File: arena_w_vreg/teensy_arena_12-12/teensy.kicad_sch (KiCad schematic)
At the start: 3 parts, among them J2 Conn_01x04_Pin, J3 Conn_01x04_Pin, U13 Teensy4.1

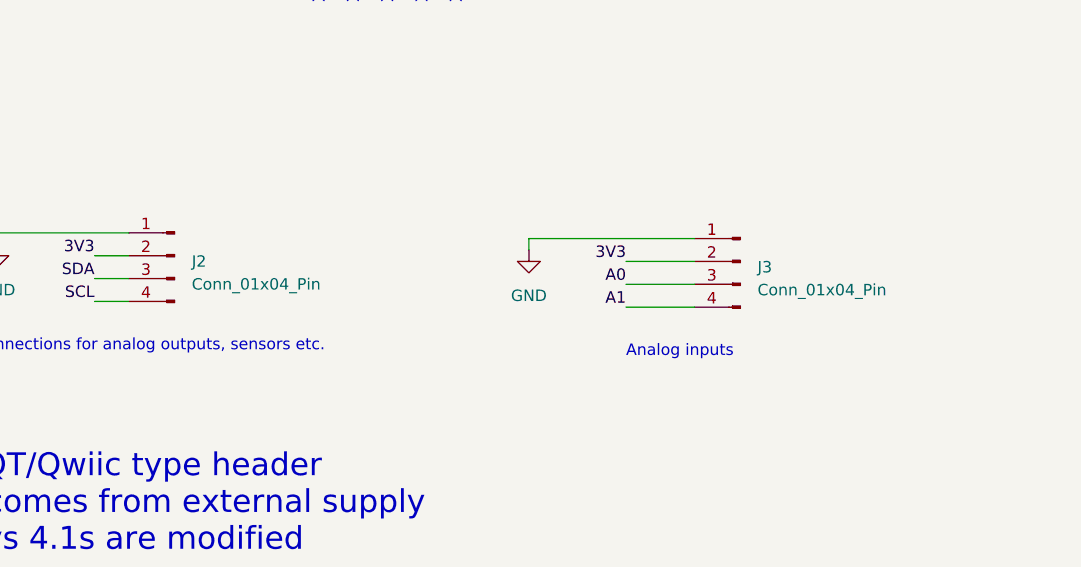
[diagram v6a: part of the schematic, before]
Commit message: Finished initial routing.
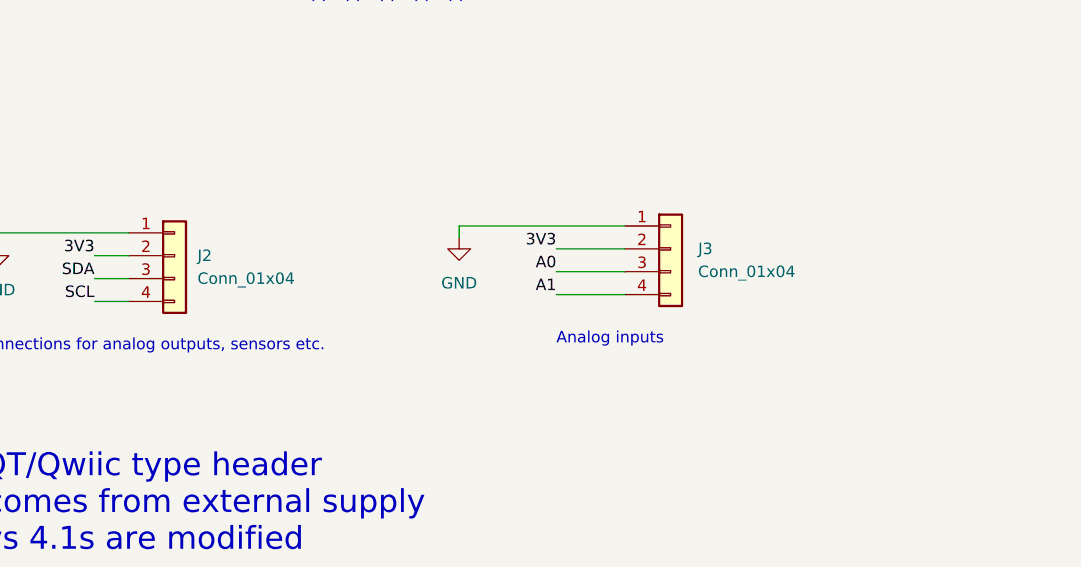
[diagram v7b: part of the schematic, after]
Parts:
- removed J2, J3: Conn_01x04_Pin, arena_custom:NS-Tech_Grove_1x04_P2mm_Horizontal, symbol Connector:Conn_01x04_Pin
- added J2, J3: Conn_01x04, Connector_JST:JST_SH_SM04B-SRSS-TB_1x04-1MP_P1.00mm_Horizontal, symbol Connector_Generic:Conn_01x04
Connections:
- net 3V3: now also J2.2 (Pin_2), J3.2 (Pin_2)
- net A0: now also J3.3 (Pin_3)
- net A1: now also J3.4 (Pin_4)
- net GND: now also J2.1 (Pin_1), J3.1 (Pin_1)
- net SCL: now also J2.4 (Pin_4)
- net SDA: now also J2.3 (Pin_3)
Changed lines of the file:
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@@
     (stroke (width 0) (type default))
   )
-  (wire (pts (xy 131.699 151.003) (xy 139.319 151.003))
+  (wire (pts (xy 123.952 149.606) (xy 131.572 149.606))
     (stroke (width 0) (type default))
   )
@@
     (stroke (width 0) (type default))
   )
-  (wire (pts (xy 120.904 148.463) (xy 120.904 149.733))
+  (wire (pts (xy 113.157 147.066) (xy 113.157 148.336))
     (stroke (width 0) (type default))
   )
@@
     (stroke (width 0) (type default))
   )
-  (wire (pts (xy 131.699 156.083) (xy 139.319 156.083))
+  (wire (pts (xy 123.952 154.686) (xy 131.572 154.686))
     (stroke (width 0) (type default))
   )
@@
     (stroke (width 0) (type default))
   )
-  (wire (pts (xy 120.904 148.463) (xy 139.319 148.463))
+  (wire (pts (xy 113.157 147.066) (xy 131.572 147.066))
     (stroke (width 0) (type default))
   )
@@
     (stroke (width 0) (type default))
   )
-  (wire (pts (xy 131.699 153.543) (xy 139.319 153.543))
+  (wire (pts (xy 123.952 152.146) (xy 131.572 152.146))
     (stroke (width 0) (type default))
   )
@@
     (effects (font (size 2.54 2.54)) (justify left bottom))
   )
-  (text "Analog inputs" (at 131.699 161.798 0)
+  (text "Analog inputs" (at 123.952 160.401 0)
     (effects (font (size 1.27 1.27)) (justify left bottom))
   )
@@
     (effects (font (size 1.27 1.27)) (justify left bottom))
   )
-  (label "3V3" (at 131.699 151.003 180) (fields_autoplaced)
+  (label "3V3" (at 123.952 149.606 180) (fields_autoplaced)
     (effects (font (size 1.27 1.27)) (justify right bottom))
   )
@@
     (effects (font (size 1.27 1.27)) (justify left bottom))
   )
-  (label "A1" (at 131.699 156.083 180) (fields_autoplaced)
+  (label "A1" (at 123.952 154.686 180) (fields_autoplaced)
     (effects (font (size 1.27 1.27)) (justify right bottom))
   )
@@
     (effects (font (size 1.27 1.27)) (justify left bottom))
   )
-  (label "A0" (at 131.699 153.543 180) (fields_autoplaced)
+  (label "A0" (at 123.952 152.146 180) (fields_autoplaced)
     (effects (font (size 1.27 1.27)) (justify right bottom))
   )
@@
     )
   )
-  (symbol (lib_id "Connector:Conn_01x04_Pin") (at 144.399 151.003 0) (mirror y) (unit 1)
+  (symbol (lib_id "Connector_Generic:Conn_01x04") (at 136.652 149.606 0) (unit 1)
     (in_bom yes) (on_board yes) (dnp no) (fields_autoplaced)
-    (property "Reference" "J3" (at 146.304 151.638 0)
-      (effects (font (size 1.27 1.27)) (justify right))
-    )
-    (property "Value" "Conn_01x04_Pin" (at 146.304 154.178 0)
-      (effects (font (size 1.27 1.27)) (justify right))
-    )
-    (property "Footprint" "arena_custom:NS-Tech_Grove_1x04_P2mm_Horizontal" (at 144.399 151.003 0)
-      (effects (font (size 1.27 1.27)) hide)
-    )
-    (property "Datasheet" "~" (at 144.399 151.003 0)
+    (property "Reference" "J3" (at 139.7 149.606 0)
+      (effects (font (size 1.27 1.27)) (justify left))
+    )
+    (property "Value" "Conn_01x04" (at 139.7 152.146 0)
+      (effects (font (size 1.27 1.27)) (justify left))
+    )
+    (property "Footprint" "Connector_JST:JST_SH_SM04B-SRSS-TB_1x04-1MP_P1.00mm_Horizontal" (at 136.652 149.606 0)
+      (effects (font (size 1.27 1.27)) hide)
+    )
+    (property "Datasheet" "~" (at 136.652 149.606 0)
       (effects (font (size 1.27 1.27)) hide)
     )
@@
     (instances
       (project "teensy_arena_12-12"
-        (path "/a2511654-3a17-43f1-8b9e-c45e375533dc"
-          (reference "J3") (unit 1)
-        )
         (path "/a2511654-3a17-43f1-8b9e-c45e375533dc/5b6d0be6-08d3-404a-9e9b-565c640343d3"
           (reference "J3") (unit 1)
@@
     )
   )
-  (symbol (lib_id "Connector:Conn_01x04_Pin") (at 81.534 150.368 0) (mirror y) (unit 1)
+  (symbol (lib_id "power:GND") (at 155.448 70.866 0) (mirror y) (unit 1)
     (in_bom yes) (on_board yes) (dnp no) (fields_autoplaced)
-    (property "Reference" "J2" (at 83.439 151.003 0)
-      (effects (font (size 1.27 1.27)) (justify right))
-    )
-    (property "Value" "Conn_01x04_Pin" (at 83.439 153.543 0)
-      (effects (font (size 1.27 1.27)) (justify right))
-    )
-    (property "Footprint" "arena_custom:NS-Tech_Grove_1x04_P2mm_Horizontal" (at 81.534 150.368 0)
+    (property "Reference" "#PWR06" (at 155.448 77.216 0)
+      (effects (font (size 1.27 1.27)) hide)
+    )
+    (property "Value" "GND" (at 155.448 75.946 0)
+      (effects (font (size 1.27 1.27)))
+    )
+    (property "Footprint" "" (at 155.448 70.866 0)
+      (effects (font (size 1.27 1.27)) hide)
+    )
+    (property "Datasheet" "" (at 155.448 70.866 0)
+      (effects (font (size 1.27 1.27)) hide)
+    )
+    (pin "1")
+    (instances
+      (project "teensy_arena_12-12"
+        (path "/a2511654-3a17-43f1-8b9e-c45e375533dc"
+          (reference "#PWR06") (unit 1)
+        )
+        (path "/a2511654-3a17-43f1-8b9e-c45e375533dc/5b6d0be6-08d3-404a-9e9b-565c640343d3"
+          (reference "#PWR016") (unit 1)
+        )
+      )
+    )
+  )
+  (symbol (lib_id "Connector_Generic:Conn_01x04") (at 81.534 150.368 0) (unit 1)
+    (in_bom yes) (on_board yes) (dnp no) (fields_autoplaced)
+    (property "Reference" "J2" (at 84.074 150.368 0)
+      (effects (font (size 1.27 1.27)) (justify left))
+    )
+    (property "Value" "Conn_01x04" (at 84.074 152.908 0)
+      (effects (font (size 1.27 1.27)) (justify left))
+    )
+    (property "Footprint" "Connector_JST:JST_SH_SM04B-SRSS-TB_1x04-1MP_P1.00mm_Horizontal" (at 81.534 150.368 0)
       (effects (font (size 1.27 1.27)) hide)
     )
@@
     (instances
       (project "teensy_arena_12-12"
-        (path "/a2511654-3a17-43f1-8b9e-c45e375533dc"
-          (reference "J2") (unit 1)
-        )
         (path "/a2511654-3a17-43f1-8b9e-c45e375533dc/5b6d0be6-08d3-404a-9e9b-565c640343d3"
           (reference "J2") (unit 1)
-        )
-      )
-    )
-  )
-  (symbol (lib_id "power:GND") (at 155.448 70.866 0) (mirror y) (unit 1)
-    (in_bom yes) (on_board yes) (dnp no) (fields_autoplaced)
-    (property "Reference" "#PWR06" (at 155.448 77.216 0)
-      (effects (font (size 1.27 1.27)) hide)
-    )
-    (property "Value" "GND" (at 155.448 75.946 0)
-      (effects (font (size 1.27 1.27)))
-    )
-    (property "Footprint" "" (at 155.448 70.866 0)
-      (effects (font (size 1.27 1.27)) hide)
-    )
-    (property "Datasheet" "" (at 155.448 70.866 0)
-      (effects (font (size 1.27 1.27)) hide)
-    )
-    (pin "1")
-    (instances
-      (project "teensy_arena_12-12"
-        (path "/a2511654-3a17-43f1-8b9e-c45e375533dc"
-          (reference "#PWR06") (unit 1)
-        )
-        (path "/a2511654-3a17-43f1-8b9e-c45e375533dc/5b6d0be6-08d3-404a-9e9b-565c640343d3"
-          (reference "#PWR016") (unit 1)
         )
       )
@@
     )
   )
-  (symbol (lib_id "power:GND") (at 120.904 149.733 0) (mirror y) (unit 1)
+  (symbol (lib_id "power:GND") (at 113.157 148.336 0) (mirror y) (unit 1)
     (in_bom yes) (on_board yes) (dnp no) (fields_autoplaced)
-    (property "Reference" "#PWR07" (at 120.904 156.083 0)
-      (effects (font (size 1.27 1.27)) hide)
-    )
-    (property "Value" "GND" (at 120.904 154.813 0)
+    (property "Reference" "#PWR07" (at 113.157 154.686 0)
+      (effects (font (size 1.27 1.27)) hide)
+    )
+    (property "Value" "GND" (at 113.157 153.416 0)
       (effects (font (size 1.27 1.27)))
     )
-    (property "Footprint" "" (at 120.904 149.733 0)
-      (effects (font (size 1.27 1.27)) hide)
-    )
-    (property "Datasheet" "" (at 120.904 149.733 0)
-      (effects (font (size 1.27 1.27)) hide)
-    )
+    (property "Footprint" "" (at 113.157 148.336 0)
+      (effects (font (size 1.27 1.27)) hide)
+    )
+    (property "Datasheet" "" (at 113.157 148.336 0)
+      (effects (font (size 1.27 1.27)) hide)
+    )

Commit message: Worked on routing.
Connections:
- net 3V3 is gone; now on net +3.3V: J2.2 (Pin_2), J3.2 (Pin_2)
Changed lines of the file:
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@@
+    (stroke (width 0) (type default))
+  )
+  (wire (pts (xy 72.644 146.05) (xy 72.644 150.368))
     (stroke (width 0) (type default))
   )
@@
   )
   (wire (pts (xy 150.749 82.042) (xy 133.096 82.042))
+    (stroke (width 0) (type default))
+  )
+  (wire (pts (xy 123.952 145.288) (xy 123.952 149.606))
     (stroke (width 0) (type default))
   )
@@
     (effects (font (size 1.27 1.27)) (justify left bottom))
   )
-  (label "3V3" (at 123.952 149.606 180) (fields_autoplaced)
-    (effects (font (size 1.27 1.27)) (justify right bottom))
-  )
   (label "PAN3V.MOSI_1" (at 59.563 76.962 0) (fields_autoplaced)
     (effects (font (size 1.27 1.27)) (justify left bottom))
@@
   (label "PAN3V.CS_18" (at 203.454 90.17 0) (fields_autoplaced)
     (effects (font (size 1.27 1.27)) (justify left bottom))
-  )
-  (label "3V3" (at 72.644 150.368 180) (fields_autoplaced)
-    (effects (font (size 1.27 1.27)) (justify right bottom))
   )
   (label "PAN3V.CS_13" (at 59.563 84.582 0) (fields_autoplaced)
@@
         (path "/a2511654-3a17-43f1-8b9e-c45e375533dc/5b6d0be6-08d3-404a-9e9b-565c640343d3"
           (reference "J3") (unit 1)
+        )
+      )
+    )
+  )
+  (symbol (lib_id "power:+3.3V") (at 72.644 146.05 0) (unit 1)
+    (in_bom yes) (on_board yes) (dnp no) (fields_autoplaced)
+    (property "Reference" "#PWR019" (at 72.644 149.86 0)
+      (effects (font (size 1.27 1.27)) hide)
+    )
+    (property "Value" "+3.3V" (at 72.644 142.621 0)
+      (effects (font (size 1.27 1.27)))
+    )
+    (property "Footprint" "" (at 72.644 146.05 0)
+      (effects (font (size 1.27 1.27)) hide)
+    )
+    (property "Datasheet" "" (at 72.644 146.05 0)
+      (effects (font (size 1.27 1.27)) hide)
+    )
+    (pin "1")
+    (instances
+      (project "teensy_arena_12-12"
+        (path "/a2511654-3a17-43f1-8b9e-c45e375533dc/5b6d0be6-08d3-404a-9e9b-565c640343d3"
+          (reference "#PWR019") (unit 1)
         )
       )
@@
         )
       )
+    )
+  )
+  (symbol (lib_id "power:+3.3V") (at 123.952 145.288 0) (unit 1)
+    (in_bom yes) (on_board yes) (dnp no) (fields_autoplaced)
+    (property "Reference" "#PWR020" (at 123.952 149.098 0)
+      (effects (font (size 1.27 1.27)) hide)
+    )
+    (property "Value" "+3.3V" (at 123.952 141.859 0)
+      (effects (font (size 1.27 1.27)))
+    )
+    (property "Footprint" "" (at 123.952 145.288 0)
+      (effects (font (size 1.27 1.27)) hide)
+    )
+    (property "Datasheet" "" (at 123.952 145.288 0)
+      (effects (font (size 1.27 1.27)) hide)
+    )
+    (pin "1")
+    (instances
+      (project "teensy_arena_12-12"
+        (path "/a2511654-3a17-43f1-8b9e-c45e375533dc/5b6d0be6-08d3-404a-9e9b-565c640343d3"
+          (reference "#PWR020") (unit 1)
+        )
+      )
